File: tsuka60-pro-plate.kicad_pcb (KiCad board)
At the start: 2 copper layers, 285 x 94.6 mm, 80 parts

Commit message: Finalise plate and exports
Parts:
- removed MX65, MX71: MX-NoLED, marbastlib-xp-plate-mx:Plate-MP_MX_1.25u
- removed MX67, MX69: MX-NoLED, marbastlib-xp-plate-mx:Plate-MP_MX_1u
- removed S2: MX_stab, marbastlib-xp-plate-mx:Plate-MP_MX_2u
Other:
- outline, holes or cut-outs redrawn

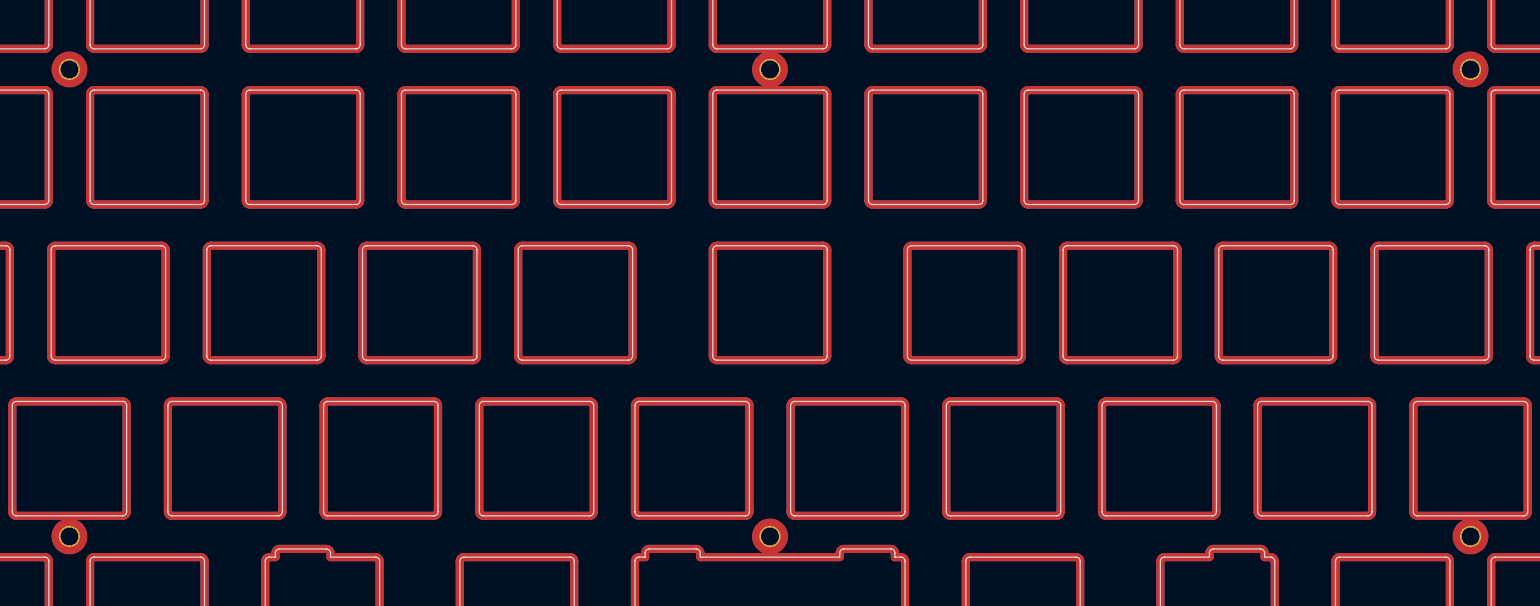
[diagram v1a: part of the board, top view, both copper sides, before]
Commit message: Adjust standoff footprint and correct orientation, produce production files
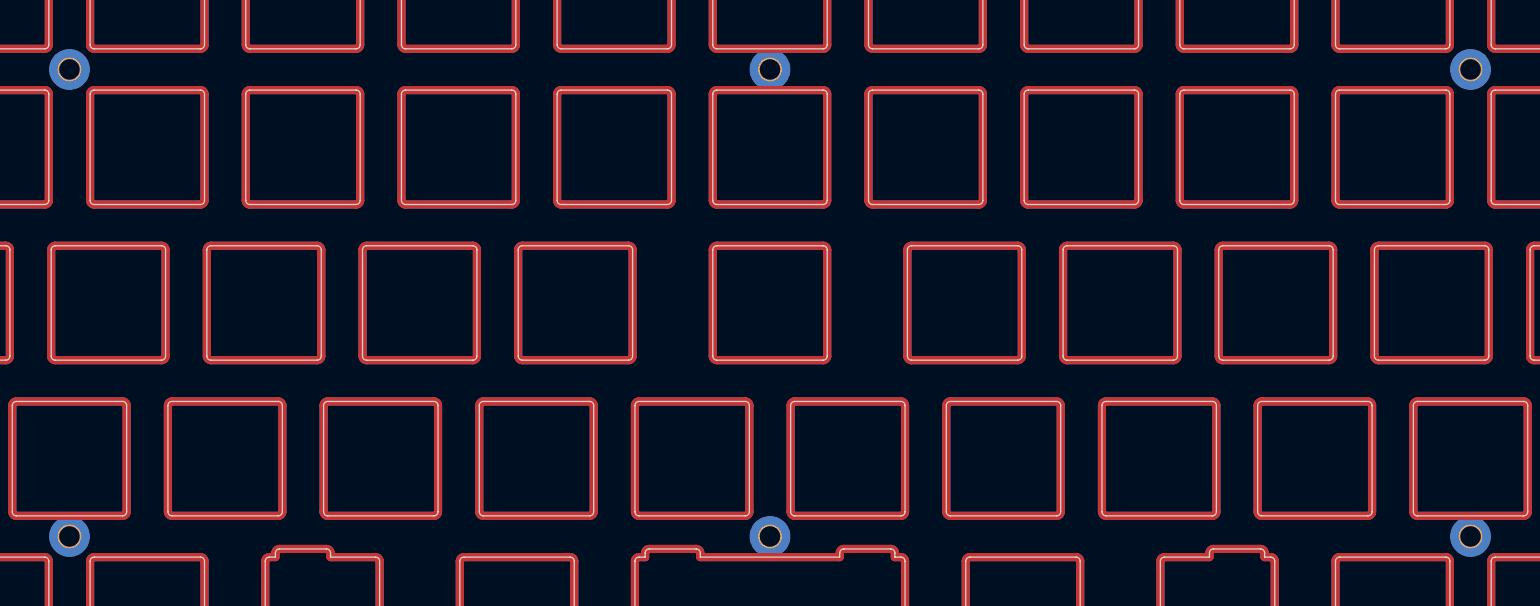
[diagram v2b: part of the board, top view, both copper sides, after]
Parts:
- H1, H2, H3, H4, H5, H6: footprint MountingHole:MountingHole_2.2mm_M2_Pad_TopOnly -> MountingHole:MountingHole_2.5mm_Pad_TopOnly; moved to B.Cu
- turned H1 to 180 degrees
- turned H2 to 180 degrees
- turned H3 to 180 degrees
- turned H4 to 180 degrees
- turned H5 to 180 degrees
- turned H6 to 180 degrees
